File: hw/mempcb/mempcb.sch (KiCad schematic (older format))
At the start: 32 parts, among them J1 RC6502_Bus, J2 0.1\" 2x25, U3 JEDEC_DIP32_RAM, U4 74LS138, U5 74LS138

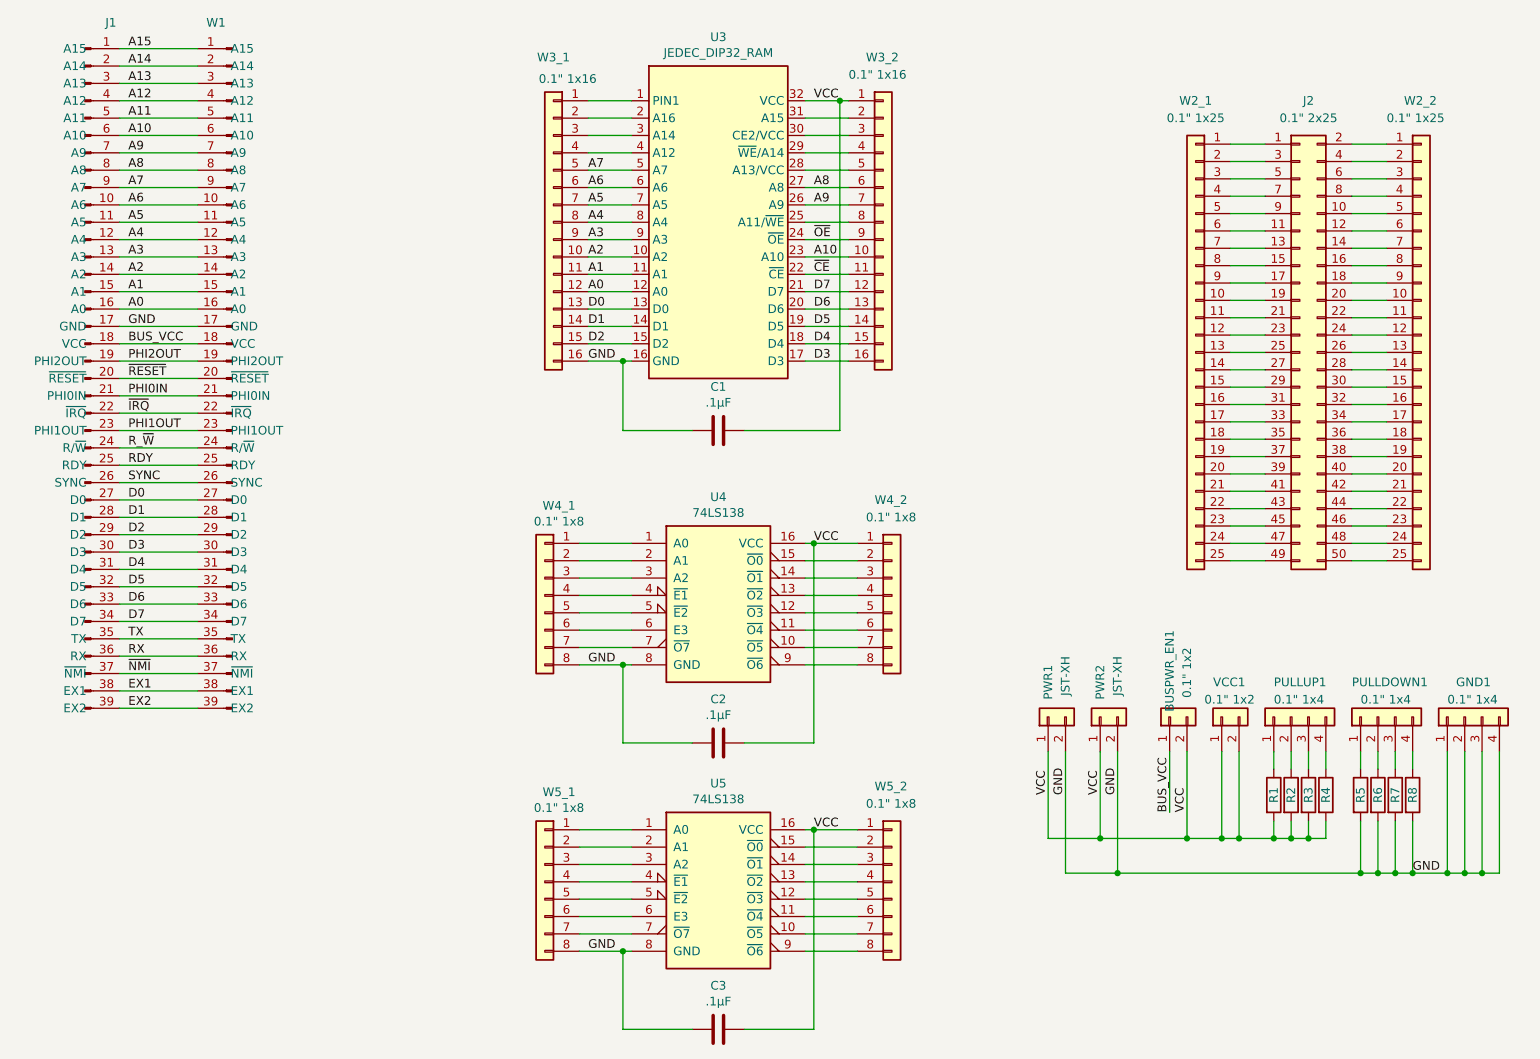
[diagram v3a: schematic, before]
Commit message: hw/mempcb: Rename most references and remove some from silkscreen
We rename the ICs to U1, U2 and U3 so that it doesn't look like some are
missing. We resolve the previous collisions with the wire-wrap headers by
renaming them all to WW_*.1 and WW_*.2 where * is the part with which
they're associated. The reference alignment and locations are also cleaned
up a bit.

Update the PCB from this, make invisible the skilk screen references for
the WW_* headers (since their associated part is easily clear from
proximity) and for the others move the silk screen to locations that are
more clear.
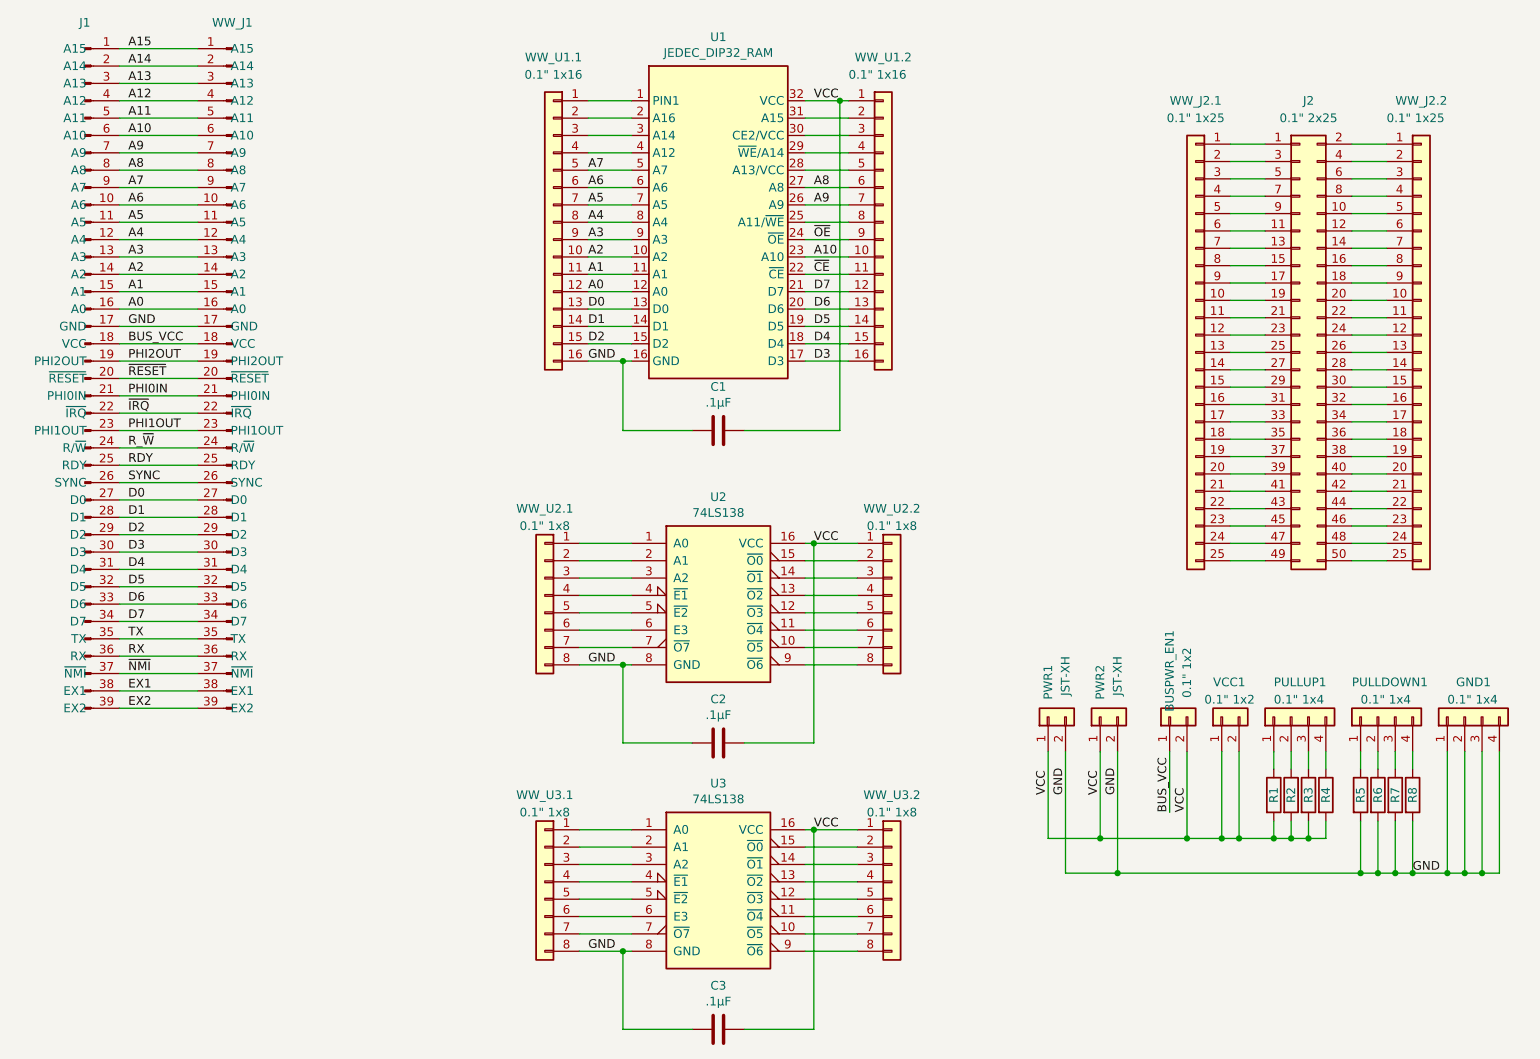
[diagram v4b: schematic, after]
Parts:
- renumbered U3 to U1, U4 to U2, U5 to U3, W1 to WW_J1, W2_1 to WW_J2.1, W2_2 to WW_J2.2, W3_1 to WW_U1.1, W3_2 to WW_U1.2, W4_1 to WW_U2.1, W4_2 to WW_U2.2, W5_1 to WW_U3.1, W5_2 to WW_U3.2
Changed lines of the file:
@@
 U 1 1 5FE89A90
 P 1850 2900
-F 0 "J1" H 2000 4950 50  0000 C CNN
+F 0 "J1" H 1850 4950 50  0000 C CNN
 F 1 "RC6502_Bus" H 1958 4890 50  0001 C CNN
 F 2 "Connector_PinHeader_2.54mm:PinHeader_1x39_P2.54mm_Vertical" H 1850 2900 50  0001 C CNN
@@
 $EndComp
 $Comp
-L mempcb:RC6502_Bus W1
+L mempcb:RC6502_Bus WW_J1
 U 1 1 5FE96F9C
 P 2700 2900
-F 0 "W1" H 2850 4950 50  0000 R CNN
+F 0 "WW_J1" H 2700 4950 50  0000 C CNN
 F 1 "RC6502_Bus" H 2300 4850 50  0001 R CNN
 F 2 "Connector_PinHeader_2.54mm:PinHeader_1x39_P2.54mm_Vertical" H 2700 2900 50  0001 C CNN
@@
 $EndComp
 $Comp
-L mempcb:JEDEC_DIP32_RAM U3
+L mempcb:JEDEC_DIP32_RAM U1
 U 1 1 5FEAD713
 P 5500 2100
-F 0 "U3" H 5500 3267 50  0000 C CNN
+F 0 "U1" H 5500 3267 50  0000 C CNN
 F 1 "JEDEC_DIP32_RAM" H 5500 3176 50  0000 C CNN
 F 2 "mempcb:DIP-32_W15.24mm_ZIF_Socket_LongPads" H 5500 2100 50  0001 C CNN
@@
 $EndComp
 $Comp
-L Connector_Generic:Conn_01x25 W2_1
+L Connector_Generic:Conn_01x25 WW_J2.1
 U 1 1 5FEB2EF1
 P 8250 2750
-F 0 "W2_1" H 8250 4200 50  0000 C CNN
+F 0 "WW_J2.1" H 8250 4200 50  0000 C CNN
 F 1 "0.1\" 1x25" H 8250 4100 50  0000 C CNN
 F 2 "Connector_PinHeader_2.54mm:PinHeader_1x25_P2.54mm_Vertical" H 8250 2750 50  0001 C CNN
@@
 $EndComp
 $Comp
-L Connector_Generic:Conn_01x25 W2_2
+L Connector_Generic:Conn_01x25 WW_J2.2
 U 1 1 5FEC1F3E
 P 9550 2750
-F 0 "W2_2" H 9450 4200 50  0000 L CNN
+F 0 "WW_J2.2" H 9550 4200 50  0000 C CNN
 F 1 "0.1\" 1x25" H 9350 4100 50  0000 L CNN
 F 2 "Connector_PinHeader_2.54mm:PinHeader_1x25_P2.54mm_Vertical" H 9550 2750 50  0001 C CNN
@@
 $EndComp
 $Comp
-L Connector_Generic:Conn_01x16 W3_1
+L Connector_Generic:Conn_01x16 WW_U1.1
 U 1 1 5FECEA90
 P 4550 2000
-F 0 "W3_1" H 4550 2950 50  0000 C CNN
-F 1 "0.1\" 1x16" H 4468 2826 50  0000 C CNN
+F 0 "WW_U1.1" H 4550 2950 50  0000 C CNN
+F 1 "0.1\" 1x16" H 4550 2850 50  0000 C CNN
 F 2 "Connector_PinHeader_2.54mm:PinHeader_1x16_P2.54mm_Vertical" H 4550 2000 50  0001 C CNN
 F 3 "~" H 4550 2000 50  0001 C CNN
@@
 $EndComp
 $Comp
-L Connector_Generic:Conn_01x08 W4_2
+L Connector_Generic:Conn_01x08 WW_U2.2
 U 1 1 5FECFD2E
 P 6500 4150
-F 0 "W4_2" H 6400 4700 50  0000 L CNN
-F 1 "0.1\" 1x8" H 6350 4600 50  0000 L CNN
+F 0 "WW_U2.2" H 6500 4650 50  0000 C CNN
+F 1 "0.1\" 1x8" H 6500 4550 50  0000 C CNN
 F 2 "Connector_PinHeader_2.54mm:PinHeader_1x08_P2.54mm_Vertical" H 6500 4150 50  0001 C CNN
 F 3 "~" H 6500 4150 50  0001 C CNN
@@
 $EndComp
 $Comp
-L Connector_Generic:Conn_01x08 W4_1
+L Connector_Generic:Conn_01x08 WW_U2.1
 U 1 1 5FED086C
 P 4500 4150
-F 0 "W4_1" H 4418 4667 50  0000 C CNN
-F 1 "0.1\" 1x8" H 4418 4576 50  0000 C CNN
+F 0 "WW_U2.1" H 4500 4650 50  0000 C CNN
+F 1 "0.1\" 1x8" H 4500 4550 50  0000 C CNN
 F 2 "Connector_PinHeader_2.54mm:PinHeader_1x08_P2.54mm_Vertical" H 4500 4150 50  0001 C CNN
 F 3 "~" H 4500 4150 50  0001 C CNN
@@
 	6250 1300 6200 1300
 $Comp
-L Connector_Generic:Conn_01x16 W3_2
+L Connector_Generic:Conn_01x16 WW_U1.2
 U 1 1 5FECF06C
 P 6450 2000
-F 0 "W3_2" H 6350 2950 50  0000 L CNN
+F 0 "WW_U1.2" H 6450 2950 50  0000 C CNN
 F 1 "0.1\" 1x16" H 6250 2850 50  0000 L CNN
 F 2 "Connector_PinHeader_2.54mm:PinHeader_1x16_P2.54mm_Vertical" H 6450 2000 50  0001 C CNN
@@
 D3
 $Comp
-L mempcb:74LS138 U4
+L mempcb:74LS138 U2
 U 1 1 5FF60AA3
 P 5500 4150
-F 0 "U4" H 5500 4717 50  0000 C CNN
+F 0 "U2" H 5500 4717 50  0000 C CNN
 F 1 "74LS138" H 5500 4626 50  0000 C CNN
 F 2 "Package_DIP:DIP-16_W7.62mm_Socket_LongPads" H 5500 4150 50  0001 C CNN
@@
 	6200 1300 6000 1300
 $Comp
-L Connector_Generic:Conn_01x08 W5_2
+L Connector_Generic:Conn_01x08 WW_U3.2
 U 1 1 5FF51E6E
 P 6500 5800
-F 0 "W5_2" H 6400 6350 50  0000 L CNN
-F 1 "0.1\" 1x8" H 6350 6250 50  0000 L CNN
+F 0 "WW_U3.2" H 6500 6300 50  0000 C CNN
+F 1 "0.1\" 1x8" H 6500 6200 50  0000 C CNN
 F 2 "Connector_PinHeader_2.54mm:PinHeader_1x08_P2.54mm_Vertical" H 6500 5800 50  0001 C CNN
 F 3 "~" H 6500 5800 50  0001 C CNN
@@
 $EndComp
 $Comp
-L Connector_Generic:Conn_01x08 W5_1
+L Connector_Generic:Conn_01x08 WW_U3.1
 U 1 1 5FF51E74
 P 4500 5800
-F 0 "W5_1" H 4418 6317 50  0000 C CNN
-F 1 "0.1\" 1x8" H 4418 6226 50  0000 C CNN
+F 0 "WW_U3.1" H 4500 6300 50  0000 C CNN
+F 1 "0.1\" 1x8" H 4500 6200 50  0000 C CNN
 F 2 "Connector_PinHeader_2.54mm:PinHeader_1x08_P2.54mm_Vertical" H 4500 5800 50  0001 C CNN
 F 3 "~" H 4500 5800 50  0001 C CNN
@@
 $EndComp
 $Comp
-L mempcb:74LS138 U5
+L mempcb:74LS138 U3
 U 1 1 5FF51E7A
 P 5500 5800
-F 0 "U5" H 5500 6367 50  0000 C CNN
+F 0 "U3" H 5500 6367 50  0000 C CNN
 F 1 "74LS138" H 5500 6276 50  0000 C CNN
 F 2 "Package_DIP:DIP-16_W7.62mm_Socket_LongPads" H 5500 5800 50  0001 C CNN
@@
 Wire Wire Line
 	5000 6100 4700 6100
-Wire Wire Line
-	5000 6200 4950 6200
-Text Label 4750 6200 0    50   ~ 0
-GND
 Text Label 6050 5500 0    50   ~ 0
 VCC
@@
 Wire Wire Line
 	4950 6650 4950 6200
-Connection ~ 4950 6200
 Wire Wire Line
 	4950 6200 4700 6200
@@
 Text Label 2100 4800 0    50   ~ 0
 EX2
+Text Label 4750 6200 0    50   ~ 0
+GND
+Wire Wire Line
+	5000 6200 4950 6200
+Connection ~ 4950 6200
 $EndSCHEMATC

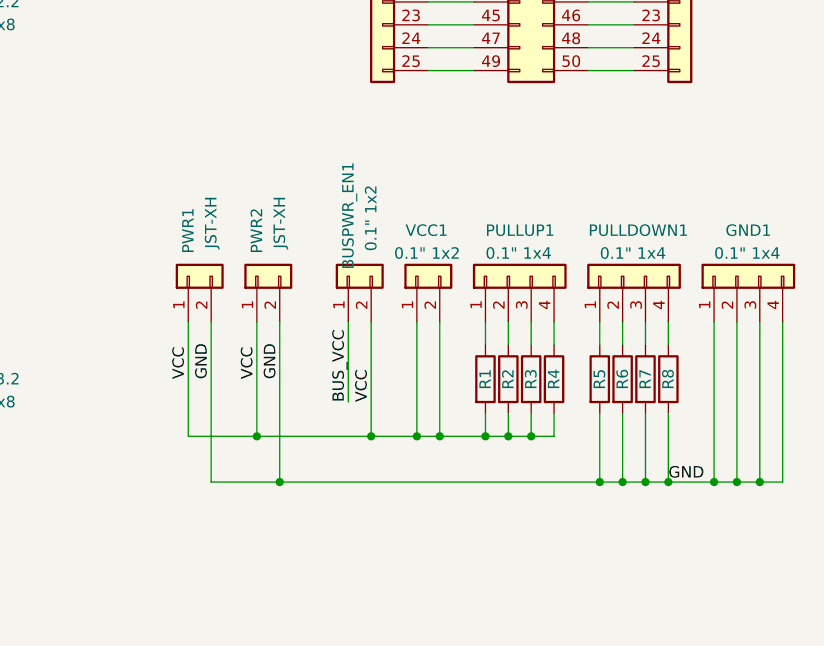
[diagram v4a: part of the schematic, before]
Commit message: hw/mempcb: Rename, rework and swap position of pull-ups/downs
- Rename PULLDOWN1 to PULLDOWN2
- Rename associated resistors to R1.1, R1.2 etc. for PULLUP1, and R2.1,
  R2.2 for PULLDOWN2.
- Make the resistor silks smaller, rotated and across the middle, so that
  they're out of the way but readable under the resistor, now now one can
  see which pins on the header they match. Nonetheless, also add pin
  numbers to the PULLDOWN2 header, since it's not lined up with the
  resistors like PULLUP1 is.
- Swap the pull-ups and pull-downs: having the pull-ups next to the power
  connectors is a bit more intuitive, and also makes for easier power
  distribution.

Also remove a couple of unconnected traces on the RC6502 header.
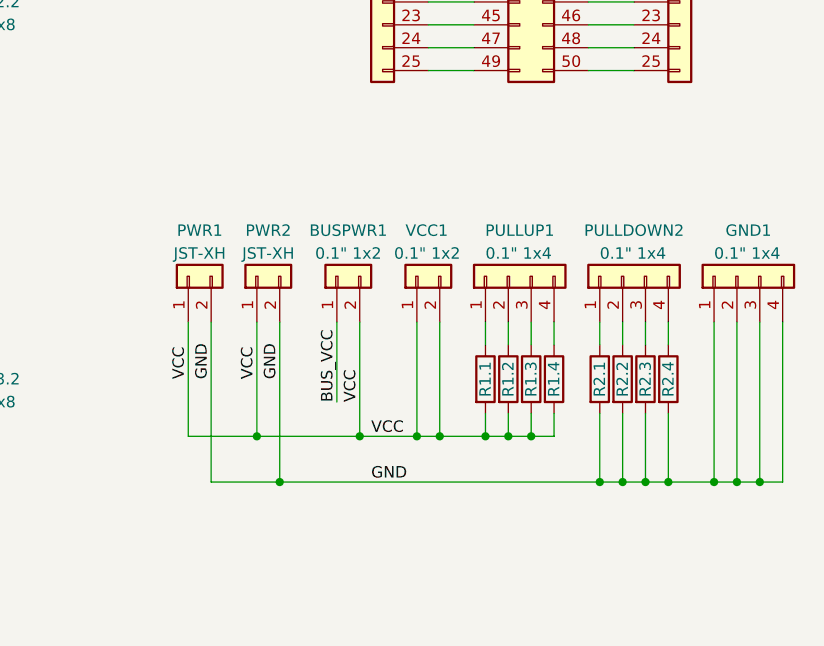
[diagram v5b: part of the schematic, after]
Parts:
- renumbered BUSPWR_EN1 to BUSPWR1, PULLDOWN1 to PULLDOWN2, R1 to R1.1, R2 to R1.2, R3 to R1.3, R4 to R1.4, R5 to R2.1, R6 to R2.2, R7 to R2.3, R8 to R2.4
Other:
- moved on the sheet: BUSPWR1
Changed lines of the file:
@@
 U 1 1 6032F1DA
 P 8800 4850
-F 0 "PULLUP1" V 9000 4950 50  0000 R CNN
+F 0 "PULLUP1" V 9000 4800 50  0000 C CNN
 F 1 "0.1\" 1x4" V 8900 4950 50  0000 R CNN
 F 2 "Connector_PinHeader_2.54mm:PinHeader_1x04_P2.54mm_Vertical" H 8800 4850 50  0001 C CNN
@@
 	8700 5150 8700 5050
 $Comp
-L Device:R R2
+L Device:R R1.2
 U 1 1 603E796E
 P 8800 5300
-F 0 "R2" V 8800 5300 50  0000 C CNN
+F 0 "R1.2" V 8800 5300 50  0000 C CNN
 F 1 "R" V 8800 5300 50  0001 C CNN
 F 2 "Resistor_THT:R_Axial_DIN0207_L6.3mm_D2.5mm_P10.16mm_Horizontal" V 8730 5300 50  0001 C CNN
@@
 	8800 5150 8800 5050
 $Comp
-L Device:R R3
+L Device:R R1.3
 U 1 1 60400026
 P 8900 5300
-F 0 "R3" V 8900 5300 50  0000 C CNN
+F 0 "R1.3" V 8900 5300 50  0000 C CNN
 F 1 "R" V 8900 5300 50  0001 C CNN
 F 2 "Resistor_THT:R_Axial_DIN0207_L6.3mm_D2.5mm_P10.16mm_Horizontal" V 8830 5300 50  0001 C CNN
@@
 	8900 5150 8900 5050
 $Comp
-L Device:R R4
+L Device:R R1.4
 U 1 1 6040C3DC
 P 9000 5300
-F 0 "R4" V 9000 5300 50  0000 C CNN
+F 0 "R1.4" V 9000 5300 50  0000 C CNN
 F 1 "R" V 9000 5300 50  0001 C CNN
 F 2 "Resistor_THT:R_Axial_DIN0207_L6.3mm_D2.5mm_P10.16mm_Horizontal" V 8930 5300 50  0001 C CNN
@@
 	8900 5550 9000 5550
 $Comp
-L Connector_Generic:Conn_01x04 PULLDOWN1
+L Connector_Generic:Conn_01x04 PULLDOWN2
 U 1 1 6042687B
 P 9300 4850
-F 0 "PULLDOWN1" V 9500 5000 50  0000 R CNN
+F 0 "PULLDOWN2" V 9500 4800 50  0000 C CNN
 F 1 "0.1\" 1x4" V 9400 4950 50  0000 R CNN
 F 2 "Connector_PinHeader_2.54mm:PinHeader_1x04_P2.54mm_Vertical" H 9300 4850 50  0001 C CNN
@@
 $EndComp
 $Comp
-L Device:R R5
+L Device:R R2.1
 U 1 1 60426881
 P 9200 5300
-F 0 "R5" V 9200 5300 50  0000 C CNN
+F 0 "R2.1" V 9200 5300 50  0000 C CNN
 F 1 "R" V 9200 5300 50  0001 C CNN
 F 2 "Resistor_THT:R_Axial_DIN0207_L6.3mm_D2.5mm_P10.16mm_Horizontal" V 9130 5300 50  0001 C CNN
@@
 	9200 5150 9200 5050
 $Comp
-L Device:R R6
+L Device:R R2.2
 U 1 1 60426889
 P 9300 5300
-F 0 "R6" V 9300 5300 50  0000 C CNN
+F 0 "R2.2" V 9300 5300 50  0000 C CNN
 F 1 "R" V 9300 5300 50  0001 C CNN
 F 2 "Resistor_THT:R_Axial_DIN0207_L6.3mm_D2.5mm_P10.16mm_Horizontal" V 9230 5300 50  0001 C CNN
@@
 	9300 5150 9300 5050
 $Comp
-L Device:R R7
+L Device:R R2.3
 U 1 1 60426891
 P 9400 5300
-F 0 "R7" V 9400 5300 50  0000 C CNN
+F 0 "R2.3" V 9400 5300 50  0000 C CNN
 F 1 "R" V 9400 5300 50  0001 C CNN
 F 2 "Resistor_THT:R_Axial_DIN0207_L6.3mm_D2.5mm_P10.16mm_Horizontal" V 9330 5300 50  0001 C CNN
@@
 	9400 5150 9400 5050
 $Comp
-L Device:R R8
+L Device:R R2.4
 U 1 1 60426899
 P 9500 5300
-F 0 "R8" V 9500 5300 50  0000 C CNN
+F 0 "R2.4" V 9500 5300 50  0000 C CNN
 F 1 "R" V 9500 5300 50  0001 C CNN
 F 2 "Resistor_THT:R_Axial_DIN0207_L6.3mm_D2.5mm_P10.16mm_Horizontal" V 9430 5300 50  0001 C CNN
@@
 	9500 5150 9500 5050
 $Comp
-L Device:R R1
+L Device:R R1.1
 U 1 1 603CD90C
 P 8700 5300
-F 0 "R1" V 8700 5300 50  0000 C CNN
+F 0 "R1.1" V 8700 5300 50  0000 C CNN
 F 1 "R" V 8700 5300 50  0001 C CNN
 F 2 "Resistor_THT:R_Axial_DIN0207_L6.3mm_D2.5mm_P10.16mm_Horizontal" V 8630 5300 50  0001 C CNN
@@
 U 1 1 604FEFCF
 P 7400 4850
-F 0 "PWR1" H 7700 4850 50  0000 R CNN
-F 1 "JST-XH" H 7750 4750 50  0000 R CNN
+F 0 "PWR1" V 7600 4900 50  0000 R CNN
+F 1 "JST-XH" V 7500 4800 50  0000 C CNN
 F 2 "Connector_JST:JST_XH_B2B-XH-A_1x02_P2.50mm_Vertical" H 7400 4850 50  0001 C CNN
 F 3 "~" H 7400 4850 50  0001 C CNN
@@
 U 1 1 6051B38D
 P 7700 4850
-F 0 "PWR2" H 8000 4850 50  0000 R CNN
-F 1 "JST-XH" H 8050 4750 50  0000 R CNN
+F 0 "PWR2" V 7900 4900 50  0000 R CNN
+F 1 "JST-XH" V 7800 4800 50  0000 C CNN
 F 2 "Connector_JST:JST_XH_B2B-XH-A_1x02_P2.50mm_Vertical" H 7700 4850 50  0001 C CNN
 F 3 "~" H 7700 4850 50  0001 C CNN
@@
 BUS_VCC
 $Comp
-L Connector_Generic:Conn_01x02 BUSPWR_EN1
+L Connector_Generic:Conn_01x02 BUSPWR1
 U 1 1 60556D43
-P 8100 4850
-F 0 "BUSPWR_EN1" H 8600 4850 50  0000 R CNN
-F 1 "0.1\" 1x2" H 8500 4750 50  0000 R CNN
-F 2 "Connector_PinHeader_2.54mm:PinHeader_1x02_P2.54mm_Vertical" H 8100 4850 50  0001 C CNN
-F 3 "~" H 8100 4850 50  0001 C CNN
-	1    8100 4850
-	0    -1   -1   0
-$EndComp
-Text Label 8100 5400 1    50   ~ 0
+P 8050 4850
+F 0 "BUSPWR1" V 8250 4800 50  0000 C CNN
+F 1 "0.1\" 1x2" V 8150 4800 50  0000 C CNN
+F 2 "Connector_PinHeader_2.54mm:PinHeader_1x02_P2.54mm_Vertical" H 8050 4850 50  0001 C CNN
+F 3 "~" H 8050 4850 50  0001 C CNN
+	1    8050 4850
+	0    -1   -1   0
+$EndComp
+Text Label 8050 5400 1    50   ~ 0
 BUS_VCC
 Wire Wire Line
-	8100 5050 8100 5400
-Text Label 8200 5400 1    50   ~ 0
+	8050 5050 8050 5400
+Text Label 8150 5400 1    50   ~ 0
 VCC
 Wire Wire Line
-	8200 5550 8400 5550
-Wire Wire Line
-	8200 5050 8200 5550
+	8150 5050 8150 5550
 Wire Wire Line
 	7400 5050 7400 5550
@@
 Connection ~ 7700 5550
 Wire Wire Line
-	7700 5550 8200 5550
+	7700 5550 8150 5550
 Wire Wire Line
 	7500 5750 7800 5750
@@
 Wire Wire Line
 	9200 5450 9200 5750
-Text Label 9500 5750 0    50   ~ 0
+Text Label 8200 5750 0    50   ~ 0
 GND
 Wire Wire Line
@@
 Wire Wire Line
 	9900 5750 9800 5750
-Connection ~ 8200 5550
 $Comp
 L Connector_Generic:Conn_01x02 VCC1
@@
 	5000 6200 4950 6200
 Connection ~ 4950 6200
+Text Label 8200 5550 0    50   ~ 0
+VCC
+Connection ~ 8150 5550
+Wire Wire Line
+	8150 5550 8400 5550
 $EndSCHEMATC

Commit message: hw/mempcb: Update RC6502 bus connector footprint with our new one
TODO: There are still issues here with the names, such as the bus power pin
being misleading labeled VCC rather than BUS_VCC (it is not on the VCC
net).

(The new footprint in the library reduces the courtyard to the connector
edges so that bus headers can be adjacent without a warning and adds silks
for the signal names.)
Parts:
- J1, WW_J1: footprint Connector_PinHeader_2.54mm:PinHeader_1x39_P2.54mm_Vertical -> mempcb:RC6502_PinHeader_1x39_P2.54mm_Vertical
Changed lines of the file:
@@
 F 0 "J1" H 1850 4950 50  0000 C CNN
 F 1 "RC6502_Bus" H 1958 4890 50  0001 C CNN
-F 2 "Connector_PinHeader_2.54mm:PinHeader_1x39_P2.54mm_Vertical" H 1850 2900 50  0001 C CNN
+F 2 "mempcb:RC6502_PinHeader_1x39_P2.54mm_Vertical" H 1850 2900 50  0001 C CNN
 F 3 "~" H 1850 2900 50  0001 C CNN
 	1    1850 2900
@@
 F 0 "WW_J1" H 2700 4950 50  0000 C CNN
 F 1 "RC6502_Bus" H 2300 4850 50  0001 R CNN
-F 2 "Connector_PinHeader_2.54mm:PinHeader_1x39_P2.54mm_Vertical" H 2700 2900 50  0001 C CNN
+F 2 "mempcb:RC6502_PinHeader_1x39_P2.54mm_Vertical" H 2700 2900 50  0001 C CNN
 F 3 "~" H 2700 2900 50  0001 C CNN
 	1    2700 2900
